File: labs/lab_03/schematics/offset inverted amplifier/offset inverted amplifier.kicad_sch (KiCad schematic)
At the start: 5 parts, among them U1 MCP601

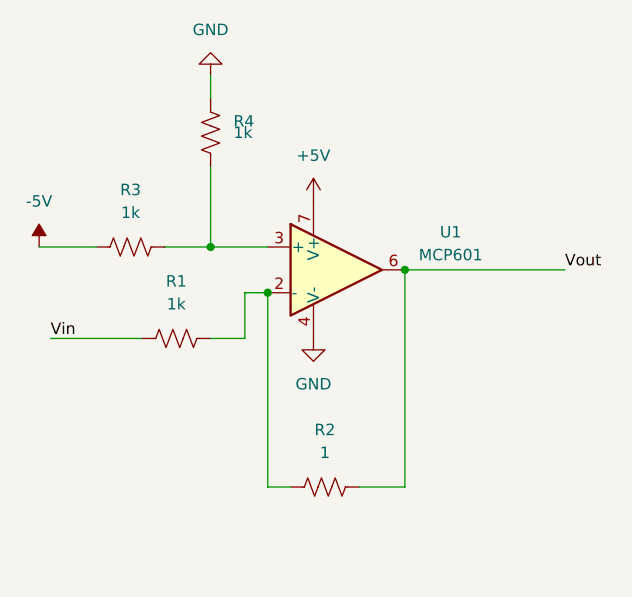
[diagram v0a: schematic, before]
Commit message: fixed inverted offset amplifier i hope
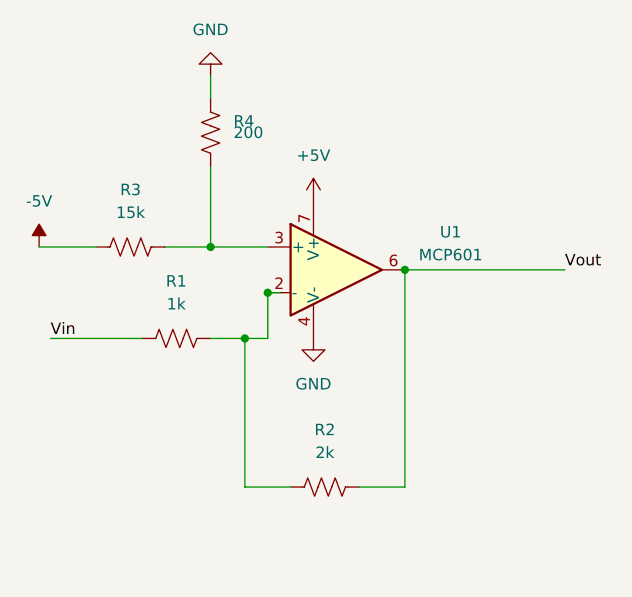
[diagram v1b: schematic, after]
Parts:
- R2: value 1 -> 2k
- R3: value 1k -> 15k
- R4: value 1k -> 200
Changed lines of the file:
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@@
     (company "E80 Team 36")
   )
+  (junction (at 132.08 91.44) (diameter 0) (color 0 0 0 0)
+  )
+  (junction (at 149.86 83.82) (diameter 0) (color 0 0 0 0)
+  )
   (junction (at 134.62 86.36) (diameter 0) (color 0 0 0 0)
   )
-  (junction (at 149.86 83.82) (diameter 0) (color 0 0 0 0)
-  )
   (junction (at 128.27 81.28) (diameter 0) (color 0 0 0 0)
   )
@@
     (stroke (width 0) (type default))
   )
+  (wire (pts (xy 128.27 91.44) (xy 132.08 91.44))
+    (stroke (width 0) (type default))
+  )
   (wire (pts (xy 123.19 81.28) (xy 128.27 81.28))
     (stroke (width 0) (type default))
   )
-  (wire (pts (xy 137.16 107.95) (xy 134.62 107.95))
+  (wire (pts (xy 134.62 91.44) (xy 134.62 86.36))
+    (stroke (width 0) (type default))
+  )
+  (wire (pts (xy 137.16 107.95) (xy 132.08 107.95))
     (stroke (width 0) (type default))
   )
@@
     (stroke (width 0) (type default))
   )
-  (wire (pts (xy 134.62 107.95) (xy 134.62 86.36))
+  (wire (pts (xy 132.08 91.44) (xy 134.62 91.44))
+    (stroke (width 0) (type default))
+  )
+  (wire (pts (xy 132.08 107.95) (xy 132.08 91.44))
     (stroke (width 0) (type default))
   )
@@
     (stroke (width 0) (type default))
   )
+  (wire (pts (xy 135.89 86.36) (xy 134.62 86.36))
+    (stroke (width 0) (type default))
+  )
   (wire (pts (xy 128.27 81.28) (xy 134.62 81.28))
     (stroke (width 0) (type default))
   )
-  (wire (pts (xy 132.08 86.36) (xy 134.62 86.36))
-    (stroke (width 0) (type default))
-  )
-  (wire (pts (xy 132.08 91.44) (xy 132.08 86.36))
-    (stroke (width 0) (type default))
-  )
   (wire (pts (xy 109.22 81.28) (xy 115.57 81.28))
     (stroke (width 0) (type default))
@@
   )
   (wire (pts (xy 110.49 91.44) (xy 120.65 91.44))
-    (stroke (width 0) (type default))
-  )
-  (wire (pts (xy 128.27 91.44) (xy 132.08 91.44))
     (stroke (width 0) (type default))
   )
@@
       (effects (font (size 1.27 1.27)))
     )
-    (property "Value" "1k" (at 119.38 77.47 90)
+    (property "Value" "15k" (at 119.38 77.47 90)
       (effects (font (size 1.27 1.27)))
     )
@@
       (effects (font (size 1.27 1.27)))
     )
-    (property "Value" "1" (at 140.97 104.14 90)
+    (property "Value" "2k" (at 140.97 104.14 90)
       (effects (font (size 1.27 1.27)))
     )
@@
       (effects (font (size 1.27 1.27)) (justify left))
     )
-    (property "Value" "1k" (at 130.81 68.58 0)
+    (property "Value" "200" (at 130.81 68.58 0)
       (effects (font (size 1.27 1.27)) (justify left))
     )

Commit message: updated inverted  offset opamp
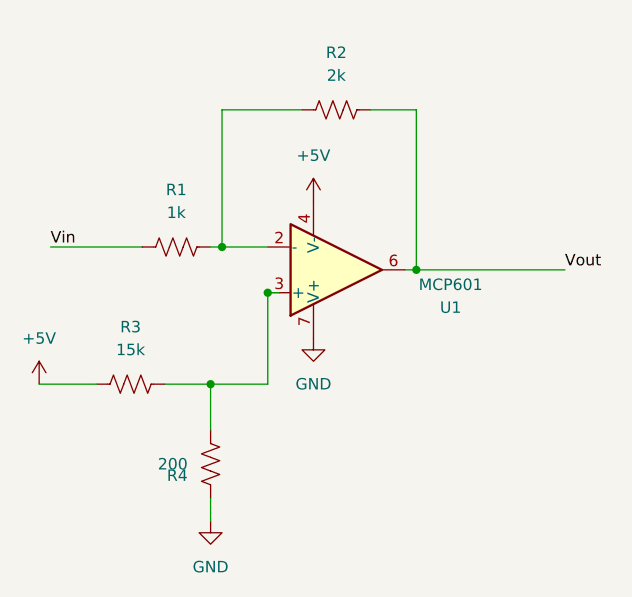
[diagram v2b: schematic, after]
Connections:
- net -5V is gone; now on net +5V: R3.1
- net +5V: now also U1.4 (V-); no longer U1.7 (V+)
- net GND: now also U1.7 (V+); no longer U1.4 (V-)
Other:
- moved on the sheet: R1, R2, R3, R4
